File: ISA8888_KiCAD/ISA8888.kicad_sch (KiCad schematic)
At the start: 6 parts, among them J1 Bus_PCI_32bit_Universal, J2 Bus_ISA_16bit, U2 AT24CS02-SSHM

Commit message: ISA8888 rev00
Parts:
- removed R1, R2: R4.7K, symbol Device:R
- added C1, C30, C33: 100uF, Capacitor_THT:CP_Radial_D5.0mm_P2.50mm, symbol Device:C_US
- added C10, C11, C12, C13, C14, C16, C17, C19, C2, C20, C21, C22, C23, C24, C25, C26, C27, C28, C29, C3, C31, C32, C4, C5, C6, C7, C8, C9: 100nF, Capacitor_SMD:C_1808_4520Metric_Pad1.72x2.30mm_HandSolder, symbol Device:C_US
- added C15, C18: 47uF, Capacitor_THT:CP_Radial_D5.0mm_P2.50mm, symbol Device:C_US
- added J3: Conn_02x03, Connector_PinHeader_2.00mm:PinHeader_2x03_P2.00mm_Vertical, symbol Connector_Generic:Conn_02x03_Odd_Even
- added J4: Conn_02x02, Connector_PinHeader_2.00mm:PinHeader_2x02_P2.00mm_Vertical, symbol Connector_Generic:Conn_02x02_Top_Bottom
- added R10, R11, R12, R9: R330, Resistor_THT:R_Axial_DIN0204_L3.6mm_D1.6mm_P5.08mm_Horizontal, symbol Device:R
- added R13, R14, R3, R4, R5, R6: R4.7K, Resistor_THT:R_Axial_DIN0204_L3.6mm_D1.6mm_P5.08mm_Horizontal, symbol Device:R
- added R15, R16, R17: R50K, Resistor_THT:R_Axial_DIN0204_L3.6mm_D1.6mm_P5.08mm_Horizontal, symbol Device:R
- added R7, R8: R1K, Resistor_THT:R_Axial_DIN0204_L3.6mm_D1.6mm_P5.08mm_Horizontal, symbol Device:R
- added RN1, RN3, RN4: R_Net_10_10k, Resistor_THT:R_Array_SIP11, symbol Device:R_Network10
- added RN2: R_Net_10_4k7, Resistor_THT:R_Array_SIP11, symbol Device:R_Network10
- added Y1: CFPS-72, Oscillator:Oscillator_SMD_IQD_IQXO70-4Pin_7.5x5.0mm, symbol Oscillator:CFPS-72
- J1: footprint (none) -> Connector_PCBEdge:BUS_PCI
- J2: footprint (none) -> ISA8888:CONN_EBC49_SUL
- U1: footprint (none) -> Package_QFP:PQFP-160_28x28mm_P0.65mm
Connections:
- net +12V: now also C13.1, C14.1, C15.1
- net +3.3V: now also C20.1, C21.1, C22.1, C23.1, C24.1, C25.1, C26.1, C27.1, C28.1, C29.1, C30.1, C31.1, R15.2, R16.2, R17.2
- net +5V: now also C1.1, C10.1, C11.1, C12.1, C2.1, C3.1, C4.1, C5.1, C6.1, C7.1, C8.1, C9.1, J4.1 (Pin_1), R10.2, R11.2, R12.2, R6.2, R7.2, R8.2, R9.2, RN2.1 (common), RN3.1 (common), RN4.1 (common), Y1.4 (+Vs)
- net -12V: now also C16.1, C17.1, C18.1
- net -5V: now also C19.1, C32.1, C33.1
- net GND: now also J1.B49 (M66EN), C1.2, C10.2, C11.2, C12.2, C13.2, C14.2, C15.2, C16.2, C17.2, C18.2, C19.2, C2.2, C20.2, C21.2, C22.2, C23.2, C24.2, C25.2, C26.2, C27.2, C28.2, C29.2, C3.2, C30.2, C31.2, C32.2, C33.2, C4.2, C5.2, C6.2, C7.2, C8.2, C9.2, J4.2 (Pin_2), R3.2, R4.2, R5.2, RN1.1 (common), Y1.2 (GND)
- net SCL: now also U1.34 (SCLK), R14.1, R14.2
- net SDA: now also U1.33 (SDATA), R13.1, R13.2
- net PCIRST#: now reaches J1.A15 (~{RST#})
- net PCIRST#: now also U1.135 (PCIRST#)
- net IGNT#: now reaches J1.A17 (~{GNT#})
- net IGNT#: now also U1.138 (IGNT#), R16.1
- net AD30: now reaches J1.A20 (AD[30])
- net AD30: now also U1.141 (AD30)
- net AD28: now reaches J1.A22 (AD[28])
- net AD28: now also U1.143 (AD28)
- net AD26: now reaches J1.A23 (AD[26])
- net AD26: now also U1.145 (AD26)
- net AD24: now reaches J1.A25 (AD[24])
- net AD24: now also U1.149 (AD24)
- net IDSEL: now reaches J1.A26 (IDSEL)
- net IDSEL: now also U1.151 (IDSEL)
- net AD22: now reaches J1.A28 (AD[22])
- net AD22: now also U1.153 (AD22)
- net AD20: now reaches J1.A29 (AD[20])
- net AD20: now also U1.155 (AD20)
- net AD18: now reaches J1.A31 (AD[18])
- net AD18: now also U1.157 (AD18)
- net AD16: now reaches J1.A32 (AD[16])
- net AD16: now also U1.159 (AD16)
- net FRAME#: now reaches J1.A34 (~{FRAME#})
- net FRAME#: now also U1.3 (FRAME#)
- net TRDY#: now reaches J1.A36 (~{TRDY#})
- net TRDY#: now also U1.5 (TRDY#)
- net STOP#: now reaches J1.A38 (~{STOP#})
- net STOP#: now also U1.7 (STOP#)
- net PAR: now reaches J1.A43 (PAR)
- net PAR: now also U1.11 (PAR)
- net AD15: now reaches J1.A44 (AD[15])
- net AD15: now also U1.13 (AD15)
- net AD13: now reaches J1.A46 (AD[13])
- net AD13: now also U1.15 (AD13)
- net AD11: now reaches J1.A47 (AD[11])
- net AD11: now also U1.17 (AD11)
- net AD9: now reaches J1.A49 (AD[09])
- net AD9: now also U1.20 (AD9)
- net C/BE0#: now reaches J1.A52 (~{C/BE#[0]})
- net C/BE0#: now also U1.23 (C/BE0#)
- net AD6: now reaches J1.A54 (AD[06])
- net AD6: now also U1.25 (AD6)
- net AD4: now reaches J1.A55 (AD[04])
- net AD4: now also U1.27 (AD4)
- net AD2: now reaches J1.A57 (AD[02])
- net AD2: now also U1.30 (AD2)
- net AD0: now reaches J1.A58 (AD[00])
- net AD0: now also U1.32 (AD0)
- net PCICLK: now reaches J1.B16 (CLK)
- net PCICLK: now also U1.137 (PCICLK)
- net IREQ#: now reaches J1.B18 (~{REQ#})
- net IREQ#: now also U1.139 (IREQ#)
- net AD31: now reaches J1.B20 (AD[31])
- net AD31: now also U1.140 (AD31)
- net AD29: now reaches J1.B21 (AD[29])
- net AD29: now also U1.142 (AD29)
- net AD27: now reaches J1.B23 (AD[27])
- net AD27: now also U1.144 (AD27)
- net AD25: now reaches J1.B24 (AD[25])
- net AD25: now also U1.147 (AD25)
- net C/BE3#: now reaches J1.B26 (C/BE#[3])
- net C/BE3#: now also U1.150 (C/BE3#)
- net AD23: now reaches J1.B27 (AD[23])
- net AD23: now also U1.152 (AD23)
- net AD21: now reaches J1.B29 (AD[21])
- net AD21: now also U1.154 (AD21)
- net AD19: now reaches J1.B30 (AD[19])
- net AD19: now also U1.156 (AD19)
- net AD17: now reaches J1.B32 (AD[17])
- net AD17: now also U1.158 (AD17)
- net C/BE2#: now reaches J1.B33 (~{C/BE#[2]})
- net C/BE2#: now also U1.2 (C/BE2#)
- net IRDY#: now reaches J1.B35 (~{IRDY#})
- net IRDY#: now also U1.4 (IRDY#)
- net DEVSEL#: now reaches J1.B37 (~{DEVSEL#})
- net DEVSEL#: now also U1.6 (DEVSEL#)
- net LOCK#: now reaches J1.B39 (~{LOCK#})
- net LOCK#: now also U1.8 (LOCK#)
- net PERR#: now reaches J1.B40 (~{PERR#})
- net PERR#: now also U1.9 (PERR#)
- net SERR#: now reaches J1.B42 (~{SERR#})
- net SERR#: now also U1.10 (SERR#)
- net C/BE1#: now reaches J1.B44 (~{C/BE#[1]})
- net C/BE1#: now also U1.12 (C/BE1#)
- net AD14: now reaches J1.B45 (AD[14])
- net AD14: now also U1.14 (AD14)
- net AD12: now reaches J1.B47 (AD[12])
- net AD12: now also U1.16 (AD12)
- net AD10: now reaches J1.B48 (AD[10])
- net AD10: now also U1.19 (AD10)
- net AD8: now reaches J1.B52 (AD[08])
- net AD8: now also U1.21 (AD8)
- net AD7: now reaches J1.B53 (AD[07])
- net AD7: now also U1.24 (AD7)
- net AD5: now reaches J1.B55 (AD[05])
- net AD5: now also U1.26 (AD5)
- net AD3: now reaches J1.B56 (AD[03])
- net AD3: now also U1.29 (AD3)
- net AD1: now reaches J1.B58 (AD[01])
- net AD1: now also U1.31 (AD1)
- net SA13: now reaches U1.100 (SA13)
- net SA13: now also J2.49 (BA13)
- net SA14: now reaches U1.102 (SA14)
- net SA14: now also J2.48 (BA14)
- net SA15: now reaches U1.103 (SA15)
- net SA15: now also J2.47 (BA15)
- net SD0: now reaches U1.104 (SD0)
- net SD0: now also J2.40 (DB0), RN3.9 (R8)
- net SD1: now reaches U1.105 (SD1)
- net SD1: now also J2.39 (DB1), RN3.8 (R7)
- net SD2: now reaches U1.106 (SD2)
- net SD2: now also J2.38 (DB2), RN3.7 (R6)
- net SD3: now reaches U1.107 (SD3)
- net SD3: now also J2.37 (DB3), RN3.6 (R5)
- net SD4: now reaches U1.108 (SD4)
- net SD4: now also J2.36 (DB4), RN3.5 (R4)
- net SD5: now reaches U1.109 (SD5)
- net SD5: now also J2.35 (DB5), RN3.4 (R3)
- net SD6: now reaches U1.110 (SD6)
- net SD6: now also J2.34 (DB6), RN3.3 (R2)
- net SD7: now reaches U1.111 (SD7)
- net SD7: now also J2.33 (DB7), RN3.2 (R1)
- net SA16: now reaches U1.112 (SA16)
- net SA16: now also J2.46 (BA16)
- net SA17: now reaches U1.113 (SA17)
- net SA17: now also J2.45 (BA17), J2.88 (LA17)
- net SA18: now reaches U1.114 (SA18)
- net SA18: now also J2.44 (BA18), J2.87 (LA18)
- net SA19: now reaches U1.115 (SA19)
- net SA19: now also J2.43 (BA19), J2.86 (LA19)
- net LA20: now reaches U1.116 (LA20)
- net LA20: now also J2.85 (LA20)
- net LA21: now reaches U1.117 (LA21)
- net LA21: now also J2.84 (LA21)
- net LA22: now reaches U1.118 (LA22)
- net LA22: now also J2.83 (LA22)
- net LA23: now reaches U1.119 (LA23)
- net LA23: now also J2.82 (LA23)
- net SD8: now reaches U1.122 (SD8)
- net SD8: now also J2.91 (D8), RN4.2 (R1)
- net SD9: now reaches U1.123 (SD9)
- net SD9: now also J2.92 (D9), RN4.3 (R2)
- net SD10: now reaches U1.124 (SD10)
- net SD10: now also J2.93 (D10), RN4.4 (R3)
- net SD11: now reaches U1.125 (SD11)
- net SD11: now also J2.94 (D11), RN4.5 (R4)
- net SD12: now reaches U1.126 (SD12)
- net SD12: now also J2.95 (D12), RN4.6 (R5)
- net SD13: now reaches U1.127 (SD13)
- net SD13: now also J2.96 (D13), RN4.7 (R6)
- net SD14: now reaches U1.128 (SD14)
- net SD14: now also J2.97 (D14), RN4.8 (R7)
- net SD15: now reaches U1.129 (SD15)
- net SD15: now also J2.98 (D15), RN4.9 (R8)
- net PPDGNT#: now reaches U1.131 (PPDGNT#)
- net PPDGNT#: now also R15.1
- net PPDREQ#: now reaches U1.132 (PPDREQ#)
- net NOGO/CLKRUN#: now reaches U1.133 (NOGO/CLKRUN#)
- net SERIRQ: now reaches U1.134 (SERIRQ)
- net SERIRQ: now also R17.1
- net RSTDRV: now reaches U1.35 (RSTDRV)
- net RSTDRV: now also J2.2 (RESET)
- net DACK7#: now reaches U1.36 (DACK7#)
- net DACK7#: now also J2.76 (~{DACK7})
- net DACK6#: now reaches U1.37 (DACK6#)
- net DACK6#: now also J2.74 (~{DACK6})
- net DACK5#: now reaches U1.38 (DACK5#)
- net DACK5#: now also J2.72 (~{DACK5})
- net DACK3#: now reaches U1.39 (DACK3#)
- net DACK3#: now also J2.15 (~{DACK3})
- net DACK2#: now reaches U1.42 (DACK2#)
- net DACK2#: now also J2.26 (~{DACK2})
- net DACK1#: now reaches U1.43 (DACK1#)
- net DACK1#: now also J2.17 (~{DACK1})
- net DACK0#: now reaches U1.44 (DACK0#)
- net DACK0#: now also J2.70 (~{DACK0})
- net DRQ7: now reaches U1.45 (DRQ7)
- net DRQ7: now also J2.77 (DRQ7), RN1.2 (R1)
- net DRQ6: now reaches U1.46 (DRQ6)
- net DRQ6: now also J2.75 (DRQ6), RN1.3 (R2)
- net DRQ5: now reaches U1.47 (DRQ5)
- net DRQ5: now also J2.73 (DRQ5), RN1.4 (R3)
- net DRQ3: now reaches U1.48 (DRQ3)
- net DRQ3: now also J2.16 (DRQ3), RN1.5 (R4)
- net DRQ2: now reaches U1.49 (DRQ2)
- net DRQ2: now also J2.6 (DRQ2), RN1.6 (R5)
- net DRQ1: now reaches U1.50 (DRQ1)
- net DRQ1: now also J2.18 (DRQ1), RN1.7 (R6)
- net DRQ0: now reaches U1.51 (DRQ0)
- net DRQ0: now also J2.71 (DRQ0), RN1.8 (R7)
- net IRQ15: now reaches U1.53 (IRQ15)
- net IRQ15: now also J2.68 (IRQ15)
- net IRQ14/ROMCS#: now reaches U1.54 (IRQ14/ROMCS#)
- net IRQ14/ROMCS#: now also J2.69 (IRQ14)
- net IRQ12: now reaches U1.55 (IRQ12)
- net IRQ12: now also J2.67 (IRQ12)
- net IRQ11: now reaches U1.56 (IRQ11)
- net IRQ11: now also J2.66 (IRQ11)
- net IRQ10: now reaches U1.57 (IRQ10)
- net IRQ10: now also J2.65 (IRQ10)
- net IRQ9: now reaches U1.58 (IRQ9)
- net IRQ7: now reaches U1.59 (IRQ7)
- net IRQ7: now also J2.21 (IRQ7)
- net IRQ6: now reaches U1.60 (IRQ6)
- net IRQ6: now also J2.22 (IRQ6)
- net IRQ5: now reaches U1.61 (IRQ5)
- net IRQ5: now also J2.23 (IRQ5)
- net IRQ4: now reaches U1.62 (IRQ4)
- net IRQ4: now also J2.24 (IRQ4)
- net IRQ3: now reaches U1.63 (IRQ3)
- net IRQ3: now also J2.25 (IRQ3)
- net TC: now reaches U1.64 (TC)
- net TC: now also J2.27 (TC), J3.5 (Pin_5)
- net REFRESH#: now reaches U1.65 (REFRESH#)
- net REFRESH#: now also J2.19 (~{REFRESH}), R8.1
- net IOCS16#: now reaches U1.66 (IOCS16#)
- net IOCS16#: now also J2.64 (~{IOCS16}), R10.1
- net MEMCS16#: now reaches U1.67 (MEMCS16#)
- net MEMCS16#: now also J2.63 (~{MEMCS16}), R11.1
- net IOCHCK#: now reaches U1.68 (IOCHCK#)
- net IOCHCK#: now also J2.32 (IO), R7.1
- net BCLK: now reaches U1.70 (BCLK)
- net BCLK: now also J2.20 (CLK)
- net IOCHRDY: now reaches U1.71 (IOCHRDY)
- net IOCHRDY: now also J2.41 (IO_READY), R6.1
- net MASTER#: now reaches U1.72 (MASTER#)
- net MASTER#: now also J2.79 (MASTER), R12.1
- net AEN: now reaches U1.73 (AEN)
- net AEN: now also J2.42 (AEN), J3.1 (Pin_1)
- net BALE: now reaches U1.74 (BALE)
- net BALE: now also J2.28 (ALE), J3.3 (Pin_3)
- net NOWS#: now reaches U1.75 (NOWS#)
- net NOWS#: now also R9.1
- net SMEMW#: now reaches U1.76 (SMEMW#)
- net SMEMW#: now also J2.11 (~{SMEMW}), RN2.5 (R4)
- net SMEMR#: now reaches U1.77 (SMEMR#)
- net SMEMR#: now also J2.12 (~{SMEMR}), RN2.4 (R3)
- net IOW#: now reaches U1.78 (IOW#)
- net IOW#: now also J2.13 (~{IOW}), RN2.3 (R2)
- net IOR#: now reaches U1.79 (IOR#)
- net IOR#: now also J2.14 (~{IOR}), RN2.2 (R1)
- net MEMW#: now reaches U1.82 (MEMW#)
- net MEMW#: now also J2.90 (~{MEMW}), RN2.7 (R6)
- net MEMR#: now reaches U1.83 (MEMR#)
- net MEMR#: now also J2.89 (~{MEMR}), RN2.6 (R5)
- net SBHE#: now reaches U1.84 (SBHE#)
- net SBHE#: now also J2.81 (SBHE)
- net SA0: now reaches U1.85 (SA0)
- net SA0: now also J2.62 (BA00)
- net SA1: now reaches U1.86 (SA1)
- net SA1: now also J2.61 (BA01)
- net SA2: now reaches U1.87 (SA2)
- net SA2: now also J2.60 (BA02)
- net SA3: now reaches U1.88 (SA3)
- net SA3: now also J2.59 (BA03)
- net SA4: now reaches U1.89 (SA4)
- net SA4: now also J2.58 (BA04)
- net SA5: now reaches U1.90 (SA5)
- net SA5: now also J2.57 (BA05)
- net SA6: now reaches U1.92 (SA6)
- net SA6: now also J2.56 (BA06)
- net SA7: now reaches U1.94 (SA7)
- net SA7: now also J2.55 (BA07)
- net SA8: now reaches U1.95 (SA8)
- net SA8: now also J2.54 (BA08)
- net SA9: now reaches U1.96 (SA9)
- net SA9: now also J2.53 (BA09)
- net SA10: now reaches U1.97 (SA10)
- net SA10: now also J2.52 (BA10)
- net SA11: now reaches U1.98 (SA11)
- net SA11: now also J2.51 (BA11)
- net SA12: now reaches U1.99 (SA12)
- net SA12: now also J2.50 (BA12)
- net OSC: now reaches J2.30 (OSC)
- net OSC: now also Y1.3 (Output)
- net 3.3VAUX: no longer names the net of J1.A14 (3.3VAUX)
- new net: J4.3 (Pin_3), J4.4 (Pin_4), Y1.1 (EN)
- new net: J3.2 (Pin_2), R3.1
- new net: J3.4 (Pin_4), R4.1
- new net: J3.6 (Pin_6), R5.1
- no-connect marks 0 -> 38
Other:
- company: (none) -> DartFrogTek (DFT)
- title: (none) -> ISA8888
- moved on the sheet: J1, J2, U1, U2

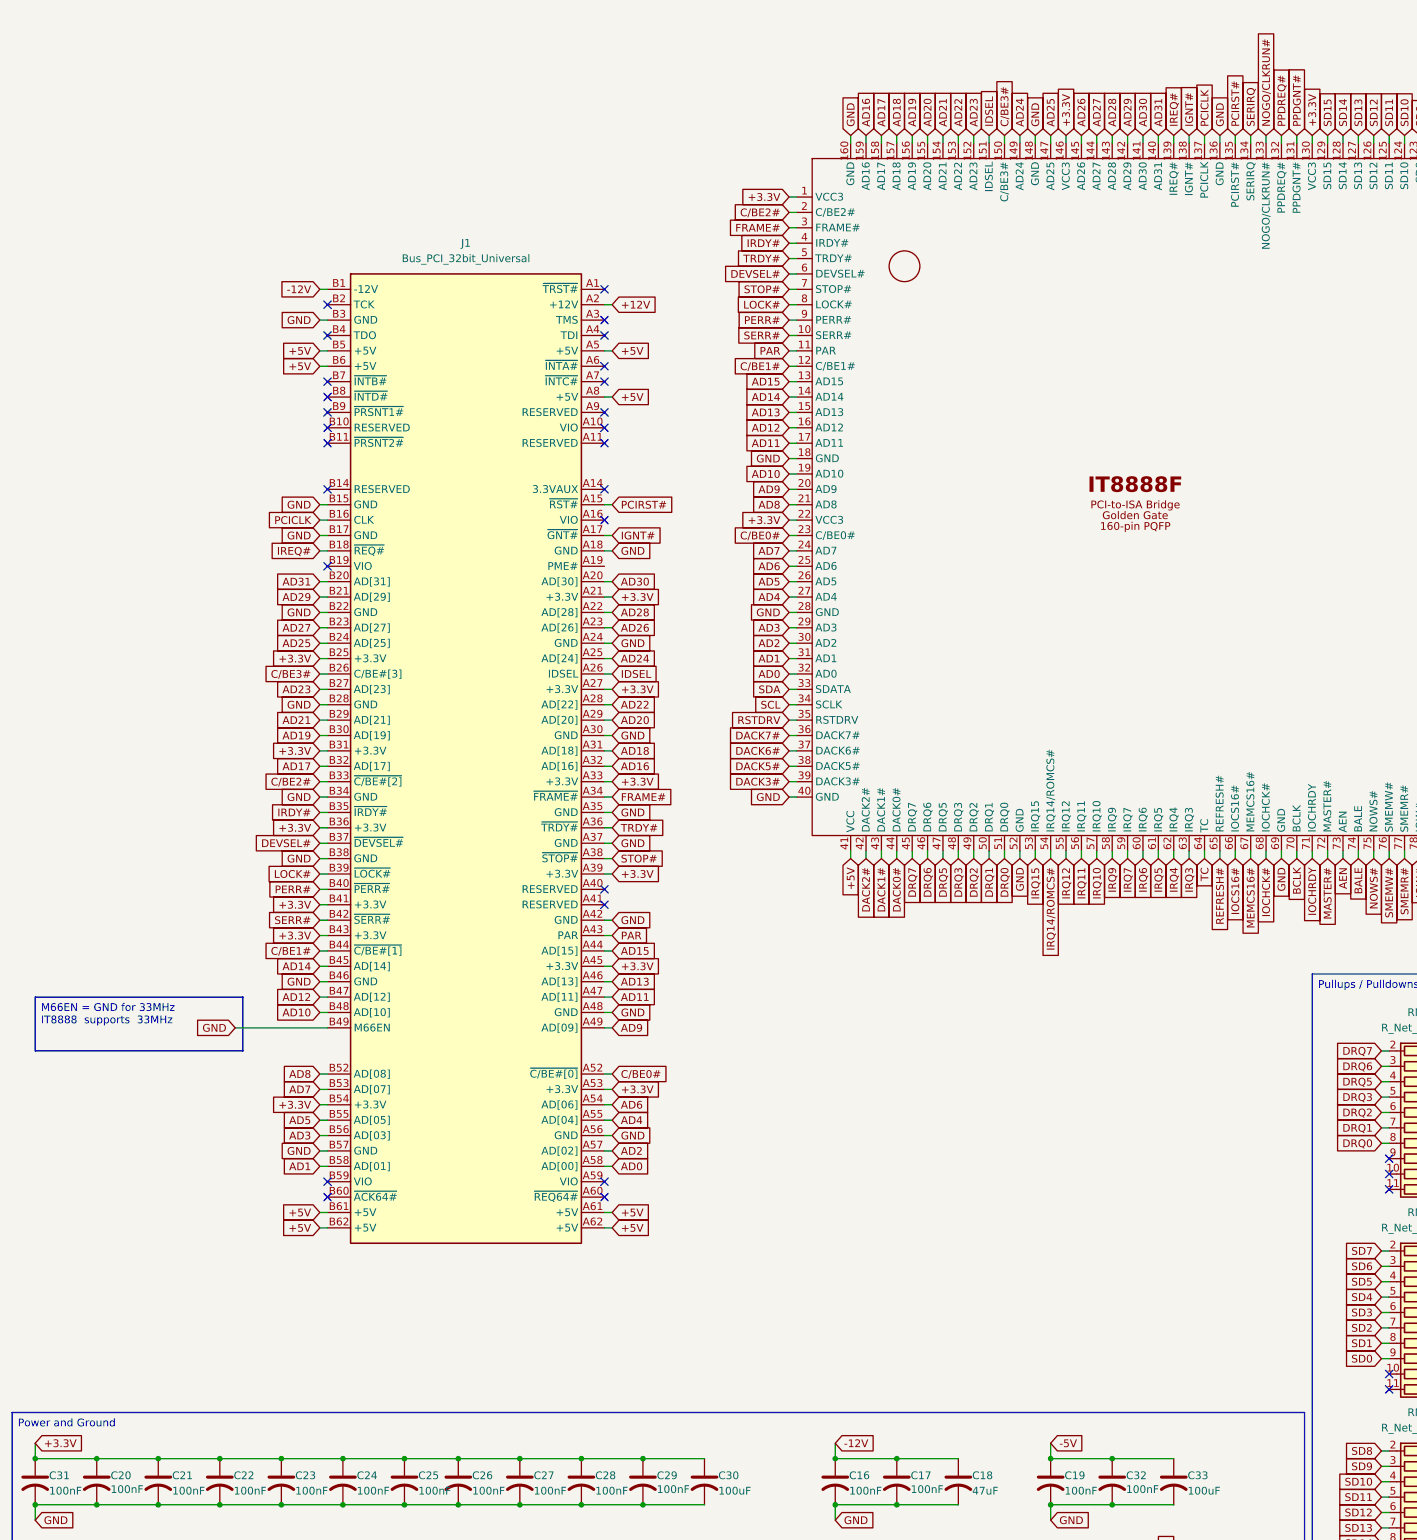
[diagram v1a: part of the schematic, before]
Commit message: Add MB PPDMA redirect and PPDMA over PCI Configuration
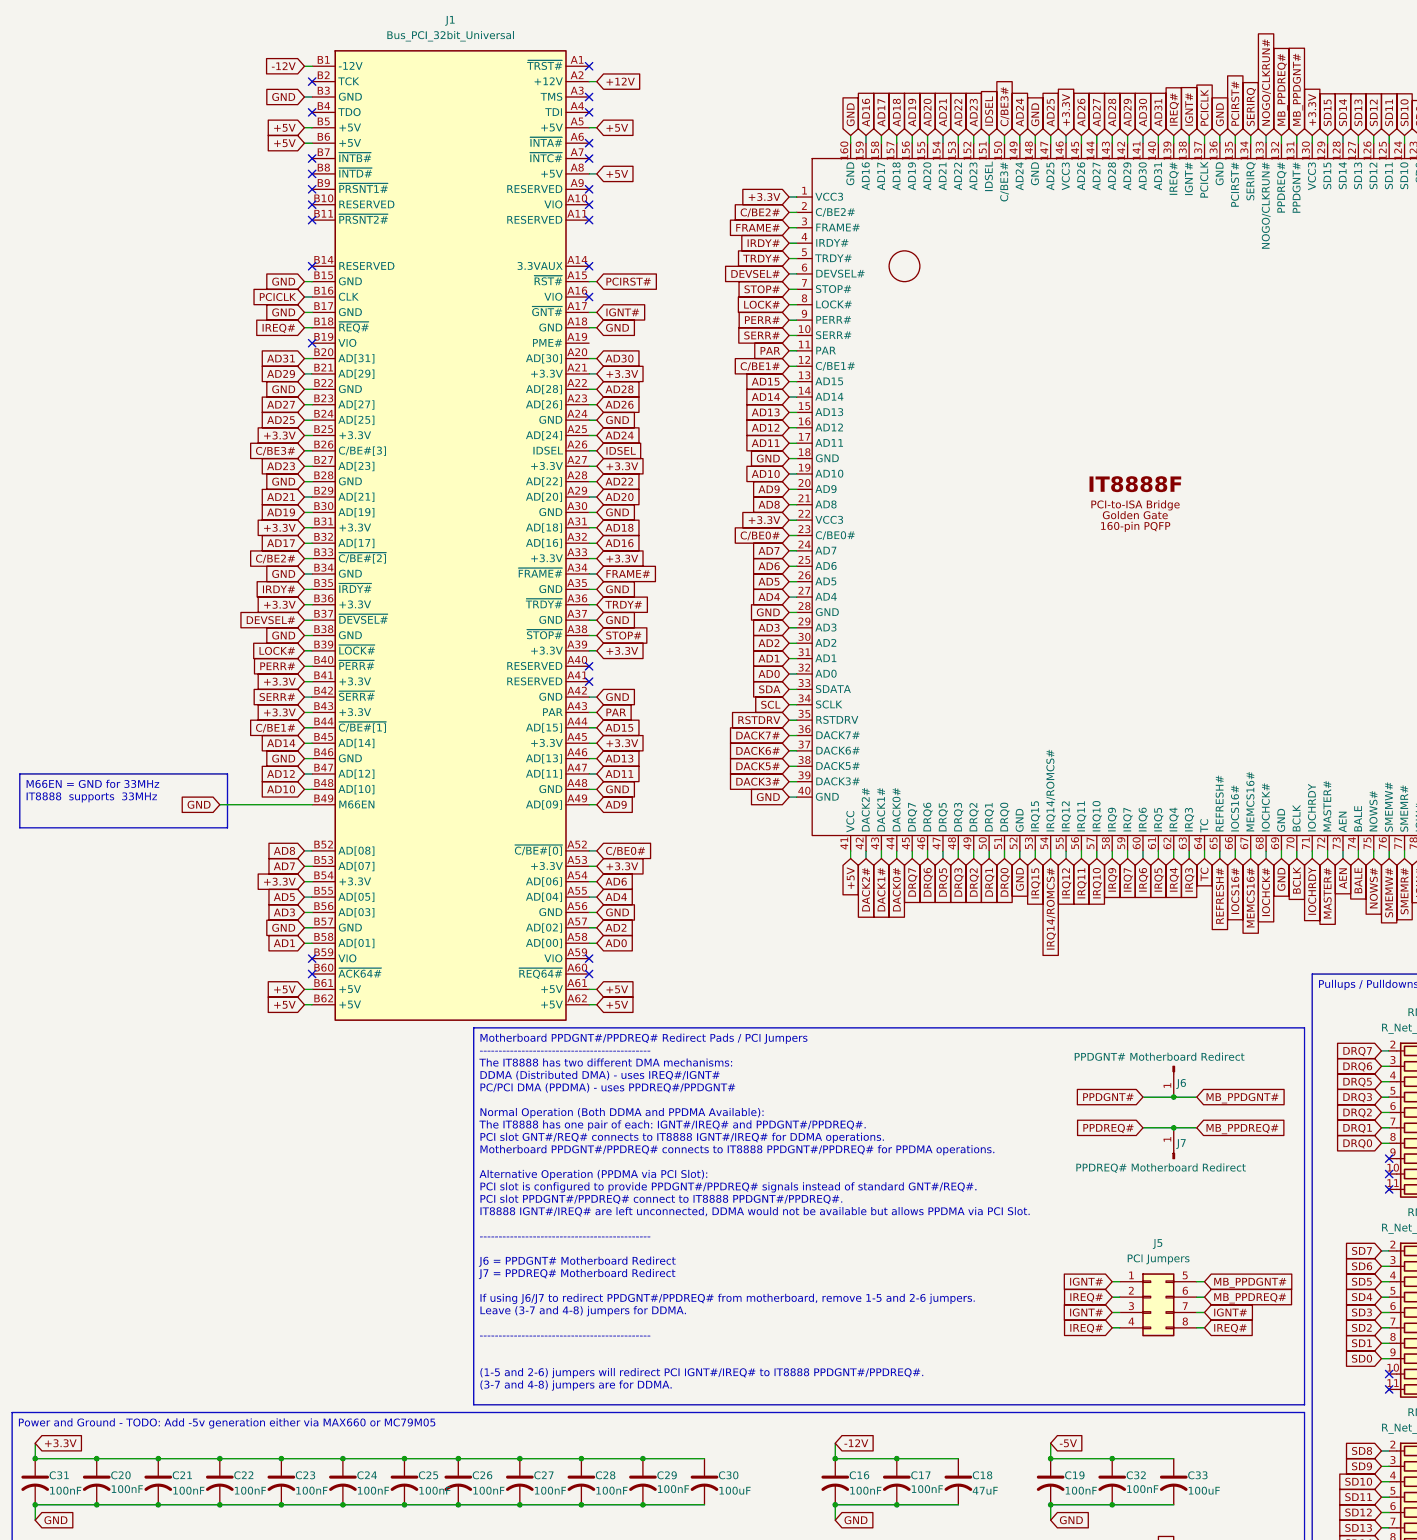
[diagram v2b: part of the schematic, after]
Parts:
- added J5: PCI Jumpers, Connector_PinHeader_2.00mm:PinHeader_2x04_P2.00mm_Vertical, symbol Connector_Generic:Conn_02x04_Top_Bottom
- added J6: PPDGNT# Motherboard Redirect, Connector_PinHeader_2.00mm:PinHeader_1x01_P2.00mm_Vertical, symbol Connector:Conn_01x01_Pin
- added J7: PPDREQ# Motherboard Redirect, Connector_PinHeader_2.00mm:PinHeader_1x01_P2.00mm_Vertical, symbol Connector:Conn_01x01_Pin
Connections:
- net IGNT#: now also J5.1 (Pin_1), J5.3 (Pin_3), J5.7 (Pin_7)
- net IREQ#: now also J5.2 (Pin_2), J5.4 (Pin_4), J5.8 (Pin_8)
- net PPDGNT# renamed MB_PPDGNT#
- net MB_PPDGNT#: now also J5.5 (Pin_5), J6.1 (Pin_1)
- net PPDREQ# renamed MB_PPDREQ#
- net MB_PPDREQ#: now also J5.6 (Pin_6), J7.1 (Pin_1)
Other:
- moved on the sheet: J1

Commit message: Routing Test + MAX660
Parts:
- added C34, C35: 150uF, Capacitor_THT:CP_Radial_D5.0mm_P2.50mm, symbol Device:C_US
- added U3: ~, Package_SO:SOIC-8_3.9x4.9mm_P1.27mm, symbol ISA8888:MAX660CSAT
- J3: value Conn_02x03 -> AEN/BALE/TC J3
- J4: value Conn_02x02 -> Crystal J4
- U2: value AT24CS02-SSHM -> SMROM-AT24CS02
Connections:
- net +5V: now also U3.8 (V+)
- net -5V: now also C35.2, U3.5 (OUT)
- net GND: now also C35.1, U3.3 (GND), U3.6 (LV)
- new net: C34.1, U3.2 (CAP+)
- new net: C34.2, U3.4 (CAP-)
- no-connect marks 38 -> 40
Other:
- note added: "PCI dISAppointment"
